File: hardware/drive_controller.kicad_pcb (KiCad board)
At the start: 2 copper layers, 71 x 19 mm, 6 parts, among them J1 Floppy Drive Connector 2x17, J2 Input, J3 Output, U1 74HC595

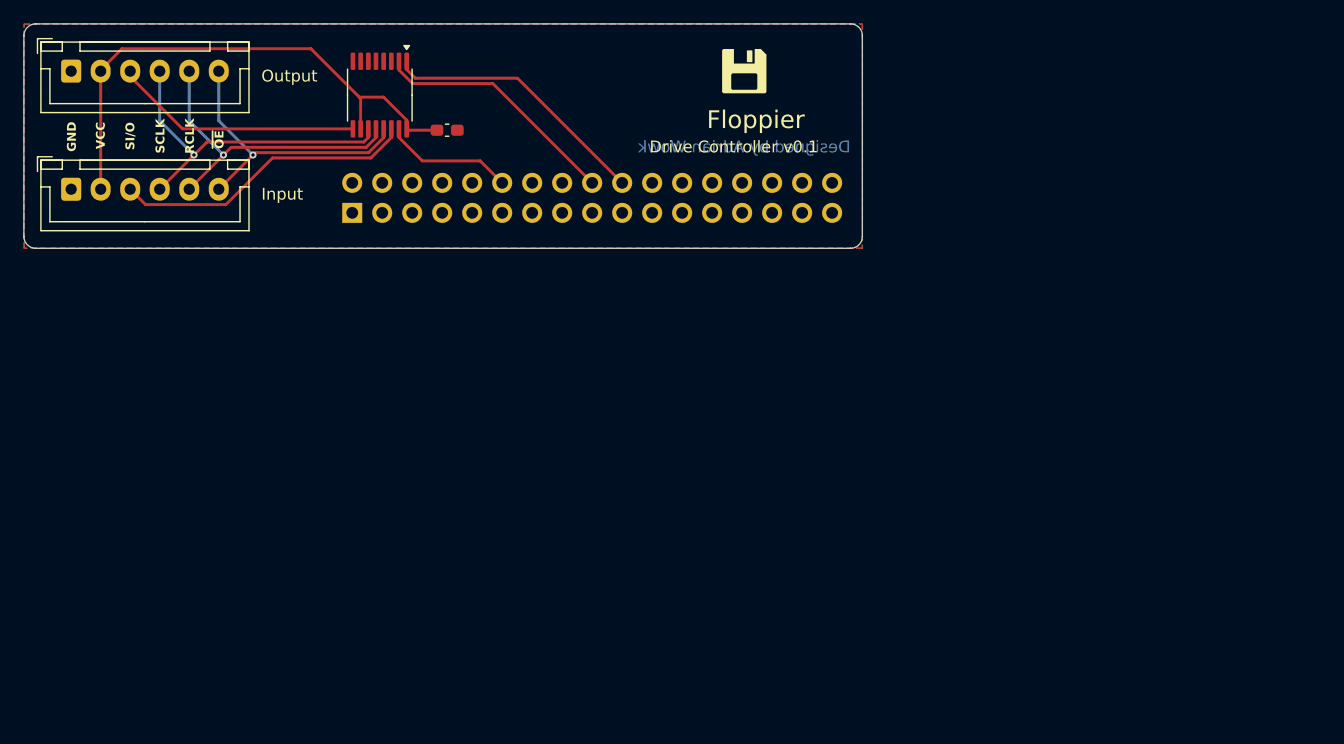
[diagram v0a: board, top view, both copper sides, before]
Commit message: refactor: update drive controller board
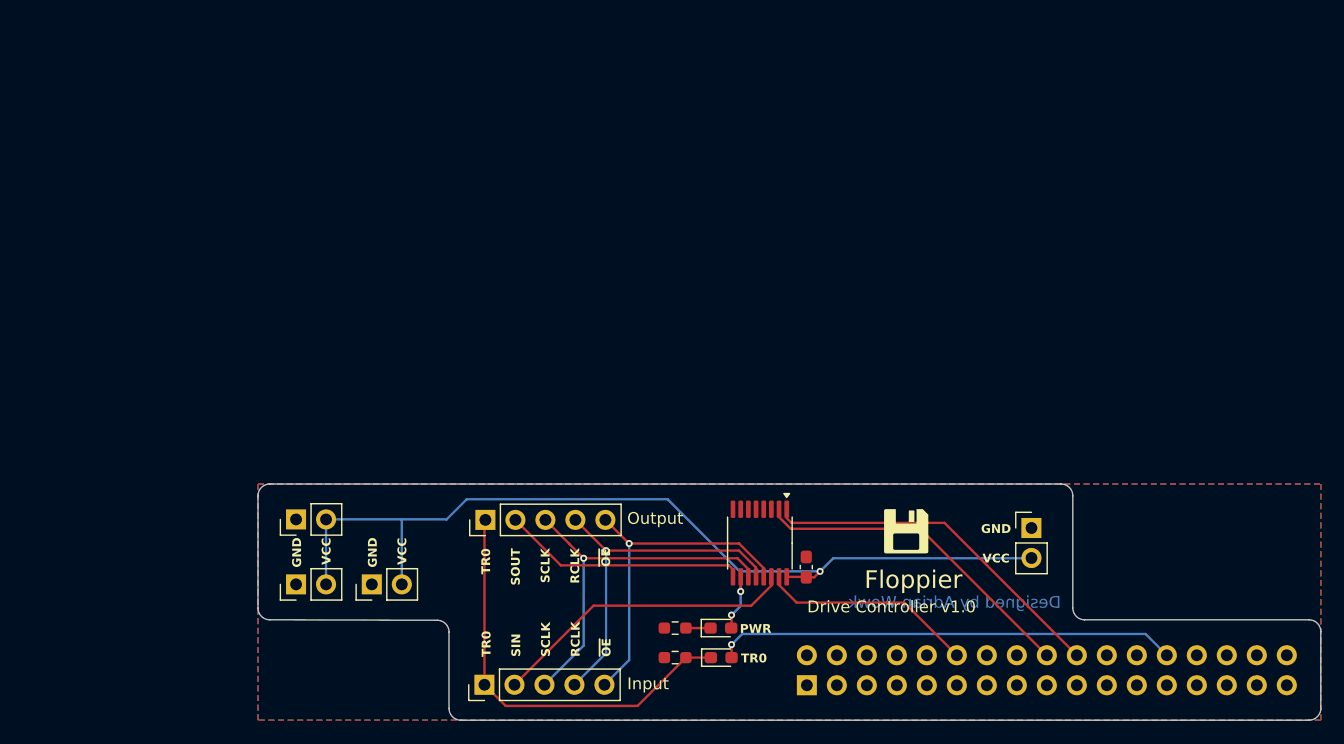
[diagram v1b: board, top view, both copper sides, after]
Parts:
- added D1: Power LED, LED_SMD:LED_0603_1608Metric_Pad1.05x0.95mm_HandSolder, F.Cu at (59.0, 32.2)
- added D2: Track 0 LED, LED_SMD:LED_0603_1608Metric_Pad1.05x0.95mm_HandSolder, F.Cu at (59.0, 34.7)
- added J4: Data Input, Connector_PinHeader_2.54mm:PinHeader_1x05_P2.54mm_Vertical, F.Cu at (39.0, 37.0)
- added J5: Data Output, Connector_PinHeader_2.54mm:PinHeader_1x05_P2.54mm_Vertical, F.Cu at (39.1, 23.0)
- added J6: Drive Power 0, Connector_PinHeader_2.54mm:PinHeader_1x02_P2.54mm_Vertical, F.Cu at (29.5, 28.5)
- added J7: Drive Power 1, Connector_PinHeader_2.54mm:PinHeader_1x02_P2.54mm_Vertical, F.Cu at (85.3, 23.7)
- added R1: 120Ω, Resistor_SMD:R_0603_1608Metric_Pad0.98x0.95mm_HandSolder, F.Cu at (55.1, 32.2)
- added R2: 120Ω, Resistor_SMD:R_0603_1608Metric_Pad0.98x0.95mm_HandSolder, F.Cu at (55.1, 34.7)
- C1: value C_Small -> 0.1uF
- J2: value Input -> Power Input; footprint Connector_JST:JST_XH_B6B-XH-A_1x06_P2.50mm_Vertical -> Connector_PinHeader_2.54mm:PinHeader_1x02_P2.54mm_Vertical
- J3: value Output -> Power Output; footprint Connector_JST:JST_XH_B6B-XH-A_1x06_P2.50mm_Vertical -> Connector_PinHeader_2.54mm:PinHeader_1x02_P2.54mm_Vertical
- moved J1 55.5 mm to (66.3, 37.0)
- moved U1 49.7 mm to (62.3, 25.0)
- moved C1 47.9 mm to (66.2, 27.0), turned to 90 degrees
- moved J3 42.5 mm to (23.0, 23.0), turned to 90 degrees
- moved G*** 41.3 mm to (74.7, 24.0)
- moved J2 38.5 mm to (23.0, 28.5), turned to 90 degrees
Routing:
- net Track 00: track 0.00 -> 39.1 mm, vias 0 -> 1
- net +5V: track 45.3 -> 83.8 mm, vias 0 -> 3
- net Track 0 OUT: track 0.00 -> 35.0 mm
- net Step: track 22.9 -> 30.1 mm
- net Drive Select 1: track 11.1 -> 18.2 mm
- net Direction Select: track 21.1 -> 28.2 mm
- net /Output Enable: track 24.8 -> 28.7 mm
- net /Store Clock: track 26.7 -> 30.2 mm
- net /Serial Clock: track 28.5 -> 31.7 mm
- net Net-(D1-K): track 0.00 -> 2.09 mm
- net /Serial Output: track 21.2 -> 20.2 mm
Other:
- board size 71 x 19 mm -> 90 x 20 mm
- board text added: "Drive Controller v1.0"
- board text added: "PWR"
- board text added: "SIN"
- board text added: "SOUT"
- board text added: "TR0"
- board text removed: "Drive Controller v0.1"
- board text removed: "SI/O"
